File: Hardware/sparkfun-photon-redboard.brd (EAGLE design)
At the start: 68.6 x 53.3 mm, 54 parts, among them J1 USB-MICROB-PTH, U1 WM-N-BM-14

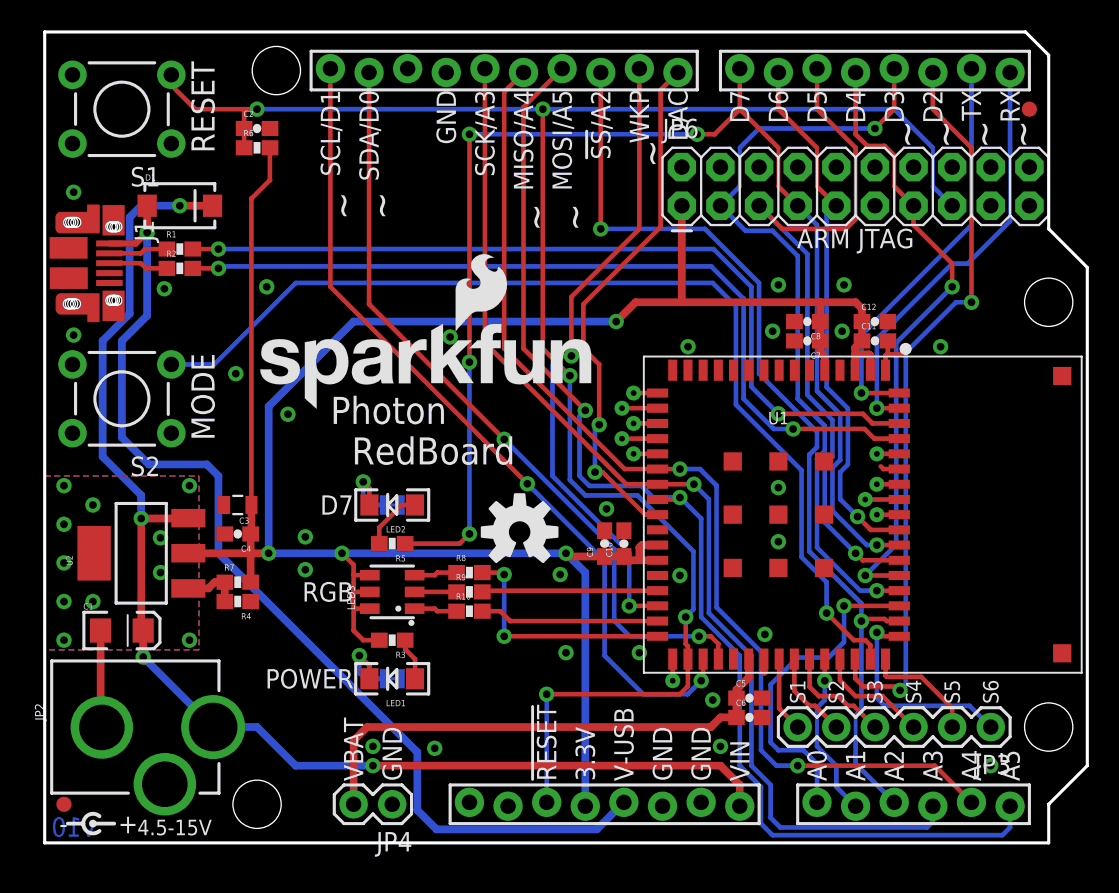
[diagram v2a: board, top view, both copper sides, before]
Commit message: Updated USB part
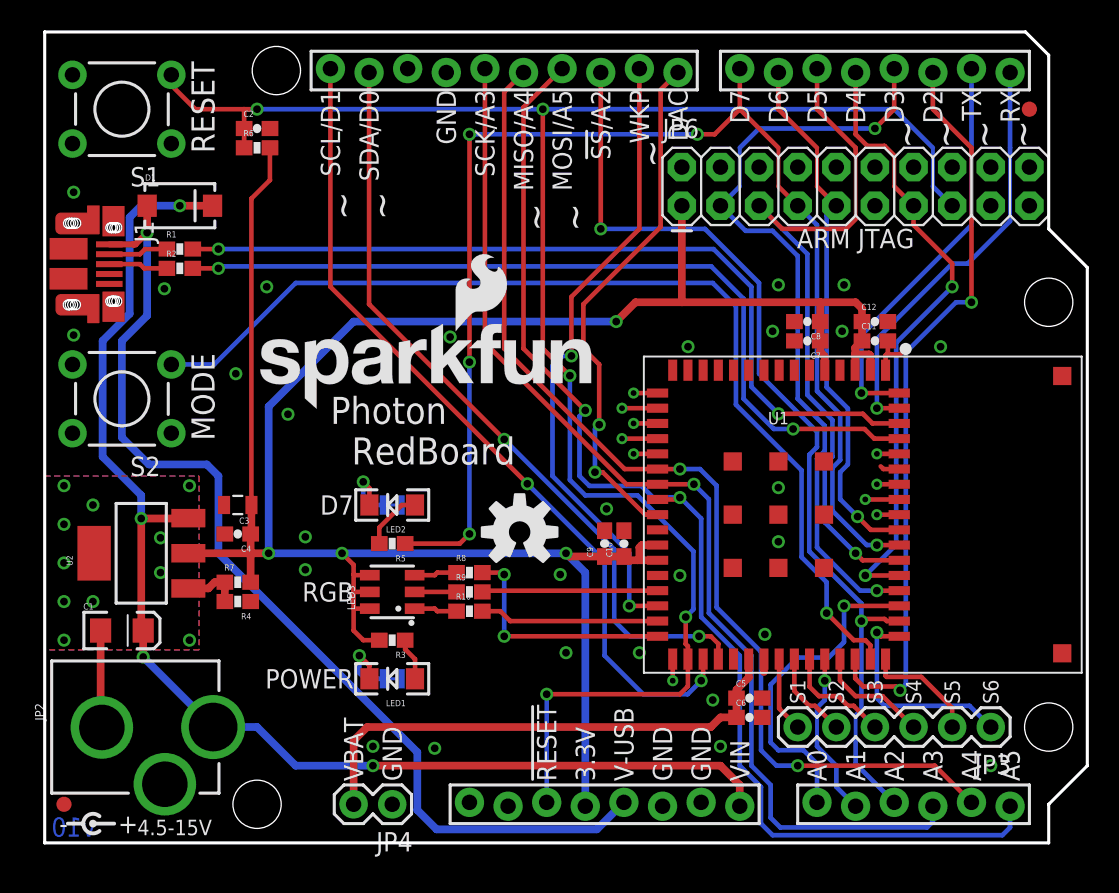
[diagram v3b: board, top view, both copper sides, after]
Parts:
- moved J1 4.90 mm to (2.92, 38.1)
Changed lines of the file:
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@@
 </class>
 </classes>
-<designrules name="SparkFun-2-layer *">
-<description language="en">&lt;b&gt;EAGLE Design Rules&lt;/b&gt;
+<designrules name="SparkFun-2-layer-TIGHT">
+<description language="en">&lt;b&gt;SparkFun 2 Layer Design Rule Checks - STANDARD/TIGHT/FAB-LIMIT&lt;/b&gt;
 &lt;p&gt;
-The default Design Rules have been set to cover
-a wide range of applications. Your particular design
-may have different requirements, so please make the
-necessary adjustments and save your customized
-design rules under a new name.</description>
+These rules have been curated by SparkFuns DFM commitee. After doing much research, communicating with our multiple fab houses, and getting quotes of various designs, we have compiled three DRU files.
+&lt;p&gt;
+&lt;b&gt;STANDARD:&lt;/b&gt; This is more of a &quot;best case scenario&quot; set of limitations. If your design has the space, and/or you have the time to work within these parameters, please do. Larger trace width and clearance makes for easier visual inspection of the PCB while troubleshooting (useful in production and to the end user). It also allows for better ability to hack a trace (if you are crazy enough to scrape away the mask and solder to a trace). Another thing to keep in mind is that more metal is just more robust.
+&lt;p&gt;
+&lt;b&gt;TIGHT:&lt;/b&gt; This is where cost comes into play. We have found that most fab houses begin to add extra charges when you go smaller than these specs. In some cases, going to less than 15 mil trace can increase the cost by 10%. (This is why we have set the min drill on this DRU to 15 mil) Same story for traces thinner than 7 mil. To avoid those extra charges, then stay within the rules of this DRU.
+&lt;p&gt;
+&lt;b&gt;FAB-LIMIT:&lt;/b&gt; These set of rules are at the very limit of most fab houses capabilities. You will pay more for these specs, and it should be used on designs that have a darned good reason to need 4 mil vias and 4 mil traces.
+&lt;p&gt;
+**NOTE Clearance, Distance, Sizes, and Restring are all set to different limits in each of these three DRU files. Please compare the files within the CAM job editor window of eagle to see all the numbers.
+&lt;p&gt;
+***NOTE, Please set your Net Classes to default (0mil for all settings), so that it won't effect the DRC when you run it with these settings.</description>
 <param name="layerSetup" value="(1*16)"/>
 <param name="mtCopper" value="0.035mm 0.035mm 0.035mm 0.035mm 0.035mm 0.035mm 0.035mm 0.035mm 0.035mm 0.035mm 0.035mm 0.035mm 0.035mm 0.035mm 0.035mm 0.035mm"/>
 <param name="mtIsolate" value="1.5mm 0.15mm 0.2mm 0.15mm 0.2mm 0.15mm 0.2mm 0.15mm 0.2mm 0.15mm 0.2mm 0.15mm 0.2mm 0.15mm 0.2mm"/>
-<param name="mdWireWire" value="8mil"/>
-<param name="mdWirePad" value="8mil"/>
-<param name="mdWireVia" value="8mil"/>
-<param name="mdPadPad" value="8mil"/>
-<param name="mdPadVia" value="8mil"/>
-<param name="mdViaVia" value="8mil"/>
-<param name="mdSmdPad" value="8mil"/>
-<param name="mdSmdVia" value="8mil"/>
-<param name="mdSmdSmd" value="8mil"/>
+<param name="mdWireWire" value="7mil"/>
+<param name="mdWirePad" value="7mil"/>
+<param name="mdWireVia" value="7mil"/>
+<param name="mdPadPad" value="7mil"/>
+<param name="mdPadVia" value="7mil"/>
+<param name="mdViaVia" value="7mil"/>
+<param name="mdSmdPad" value="7mil"/>
+<param name="mdSmdVia" value="7mil"/>
+<param name="mdSmdSmd" value="7mil"/>
 <param name="mdViaViaSameLayer" value="8mil"/>
 <param name="mnLayersViaInSmd" value="2"/>
-<param name="mdCopperDimension" value="8mil"/>
-<param name="mdDrill" value="8mil"/>
+<param name="mdCopperDimension" value="7mil"/>
+<param name="mdDrill" value="7mil"/>
 <param name="mdSmdStop" value="0mil"/>
 <param name="msWidth" value="7mil"/>
-<param name="msDrill" value="10mil"/>
+<param name="msDrill" value="15mil"/>
 <param name="msMicroVia" value="9.99mm"/>
 <param name="msBlindViaRatio" value="0.5"/>
@@
 <param name="rvMicroViaOuter" value="0.25"/>
 <param name="rvMicroViaInner" value="0.25"/>
-<param name="rlMinPadTop" value="12mil"/>
+<param name="rlMinPadTop" value="7mil"/>
 <param name="rlMaxPadTop" value="20mil"/>
-<param name="rlMinPadInner" value="10mil"/>
+<param name="rlMinPadInner" value="7mil"/>
 <param name="rlMaxPadInner" value="20mil"/>
-<param name="rlMinPadBottom" value="12mil"/>
+<param name="rlMinPadBottom" value="7mil"/>
 <param name="rlMaxPadBottom" value="20mil"/>
-<param name="rlMinViaOuter" value="10mil"/>
+<param name="rlMinViaOuter" value="7mil"/>
 <param name="rlMaxViaOuter" value="20mil"/>
-<param name="rlMinViaInner" value="10mil"/>
+<param name="rlMinViaInner" value="7mil"/>
 <param name="rlMaxViaInner" value="20mil"/>
 <param name="rlMinMicroViaOuter" value="4mil"/>
@@
 <param name="mlMinCreamFrame" value="0mil"/>
 <param name="mlMaxCreamFrame" value="0mil"/>
-<param name="mlViaStopLimit" value="20mil"/>
+<param name="mlViaStopLimit" value="25mil"/>
 <param name="srRoundness" value="0"/>
 <param name="srMinRoundness" value="0mil"/>
@@
 <element name="SJ2" library="SparkFun-Passives" package="PAD-JUMPER-2-NC_BY_TRACE_YES_SILK" value="D7-LED" x="22.86" y="22.225" rot="MR0"/>
 <element name="LOGO3" library="SparkFun-Aesthetics" package="SFE_LOGO_NAME_FLAME_.4" value="SFE_LOGO_NAME_FLAME.4_INCH" x="40.64" y="6.35" rot="MR45"/>
-<element name="J1" library="SparkFun-Connectors" package="USB-MICROB-PTH" value="USB-MICROB-PTH" x="0" y="42.037" rot="R270">
-<attribute name="PROD_ID" value="CONN-XXXXXX" x="0" y="42.037" size="1.778" layer="27" rot="R270" display="off"/>
+<element name="J1" library="SparkFun-Connectors" package="USB-MICROB-PTH" value="USB-MICROB-PTH" x="2.921" y="38.1" rot="R270">
+<attribute name="PROD_ID" value="CONN-XXXXXX" x="2.921" y="38.1" size="1.778" layer="27" rot="R270" display="off"/>
 </element>
 </elements>
@@
 <contactref element="R1" pad="1"/>
 <contactref element="J1" pad="D-"/>
-<wire x1="4.257" y1="38.777" x2="6.323" y2="38.777" width="0.3048" layer="1"/>
 <wire x1="8.04" y1="39.06" x2="6.606" y2="39.06" width="0.3048" layer="1"/>
-<wire x1="6.606" y1="39.06" x2="6.323" y2="38.777" width="0.3048" layer="1"/>
+<wire x1="6.606" y1="39.06" x2="6.26458125" y2="38.71858125" width="0.3048" layer="1"/>
+<wire x1="4.25191875" y1="38.71858125" x2="6.26458125" y2="38.71858125" width="0.3048" layer="1"/>
 </signal>
 <signal name="D+">
 <contactref element="R2" pad="1"/>
 <contactref element="J1" pad="D+"/>
-<wire x1="4.257" y1="38.127" x2="6.323" y2="38.127" width="0.3048" layer="1"/>
-<wire x1="6.323" y1="38.127" x2="6.66" y2="37.79" width="0.3048" layer="1"/>
-<wire x1="8.04" y1="37.79" x2="6.66" y2="37.79" width="0.3048" layer="1"/>
+<wire x1="8.04" y1="37.79" x2="6.5431625" y2="37.79" width="0.3048" layer="1"/>
+<wire x1="4.25191875" y1="38.06858125" x2="6.26458125" y2="38.06858125" width="0.3048" layer="1"/>
+<wire x1="6.5431625" y1="37.79" x2="6.26458125" y2="38.06858125" width="0.3048" layer="1"/>
 </signal>
 <signal name="MCU_USB_D-">
@@
 <wire x1="11.43" y1="24.13" x2="10.668" y2="24.892" width="0.508" layer="16"/>
 <contactref element="J1" pad="VBUS"/>
-<wire x1="4.257" y1="39.427" x2="5.999" y2="39.427" width="0.4064" layer="1"/>
 <wire x1="6.74" y1="40.141" x2="6.713" y2="40.141" width="0.4064" layer="1"/>
-<wire x1="6.713" y1="40.141" x2="5.999" y2="39.427" width="0.4064" layer="1"/>
+<wire x1="4.25191875" y1="39.36858125" x2="5.842" y2="39.36858125" width="0.4064" layer="1"/>
+<wire x1="5.842" y1="39.36858125" x2="5.842" y2="39.37" width="0.4064" layer="1"/>
+<wire x1="5.842" y1="39.37" x2="5.969" y2="39.37" width="0.4064" layer="1"/>
+<wire x1="5.969" y1="39.37" x2="6.74" y2="40.141" width="0.4064" layer="1"/>
 </signal>
 <signal name="VIN">

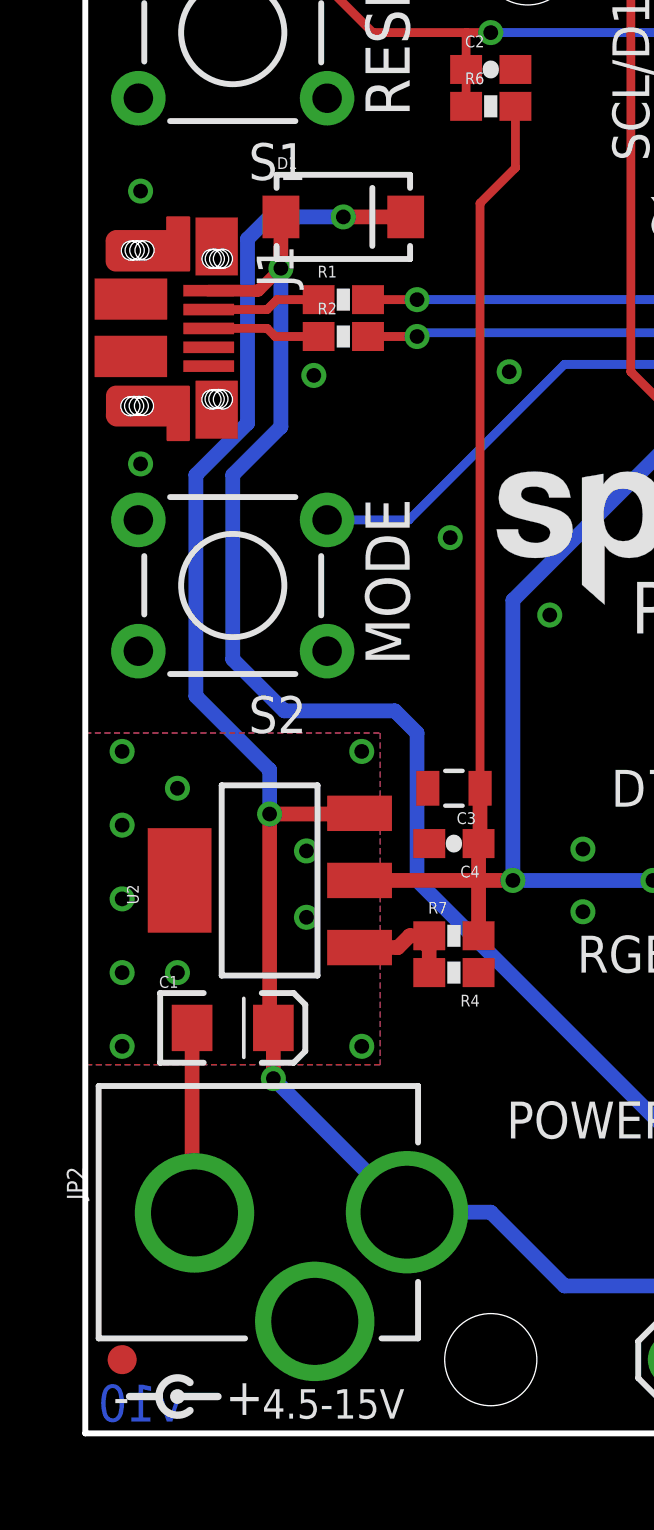
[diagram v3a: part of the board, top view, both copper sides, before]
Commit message: Updated RedBoard with new PTH USB
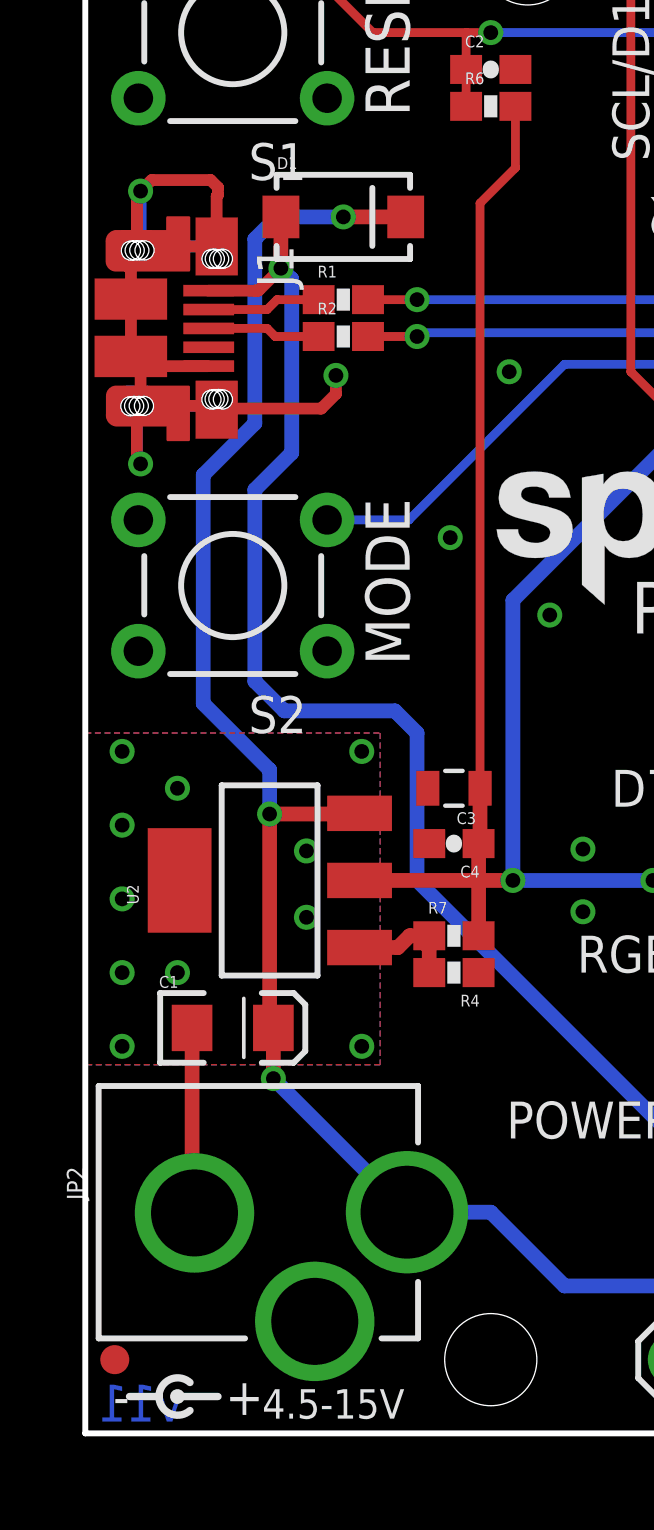
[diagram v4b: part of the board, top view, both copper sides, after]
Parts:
- J1: value USB-MICROB-PTH -> AMP FCI 10103594-0001LF
- moved FID2 0.25 mm to (1.02, 2.54)
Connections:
- net GND: now also J1.P$1, J1.P$10, J1.P$12, J1.P$2, J1.P$3, J1.P$4, J1.P$6, J1.P$8, J1.SHEILD2, J1.SHIELD3, J1.SHIELD4
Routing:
- net GND: track 11.8 -> 53.9 mm
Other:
- board text added: "v11"
- board text removed: "v10"
